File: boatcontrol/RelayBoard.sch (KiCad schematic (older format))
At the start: 15 parts, among them J2301 Conn_02x20_Odd_Even Header, J2302 TBL008V-1000-08BE, J2303 TBL008V-1000-08BE, K2301 EW60-1A3-CL12D04, K2302 EW60-1A3-CL12D04, K2303 EW60-1A3-CL12D04, K2304 EW60-1A3-CL12D04, K2305 EW60-1A3-CL12D04, K2306 EW60-1A3-CL12D04, K2307 EW60-1A3-CL12D04, K2308 EW60-1A3-CL12D04

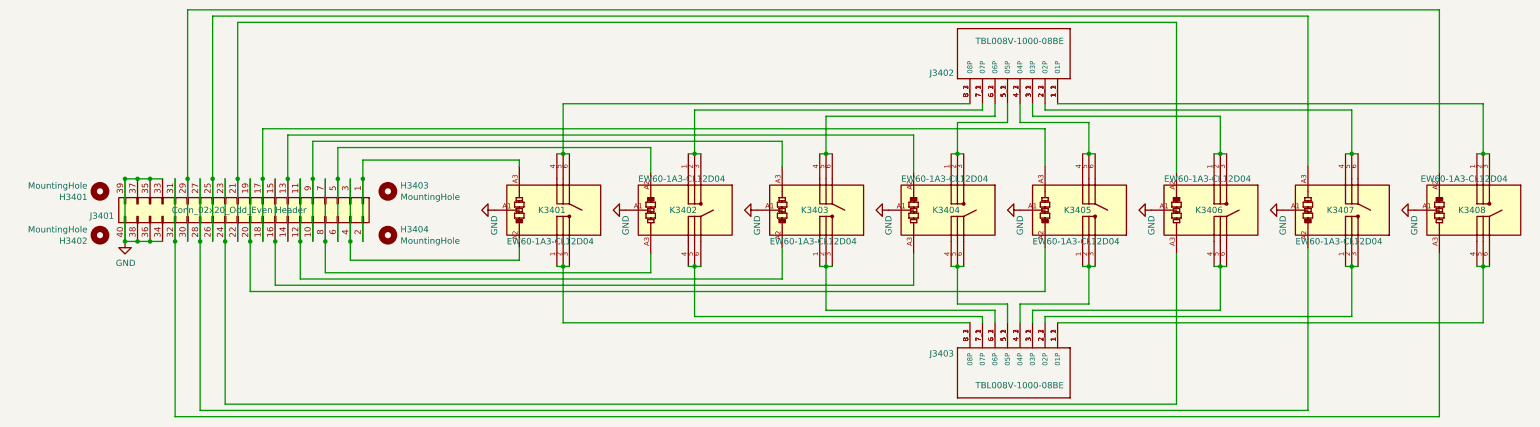
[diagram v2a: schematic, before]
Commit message: Fix extra signals
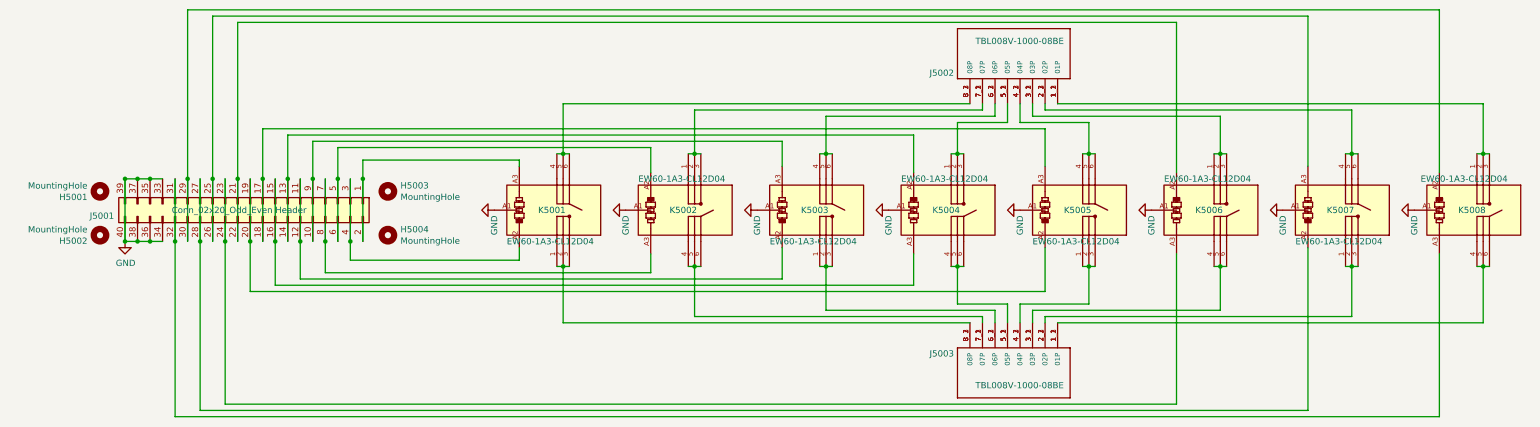
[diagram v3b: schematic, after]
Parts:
- renumbered H2301 to H5001, H2302 to H5002, H2303 to H5003, H2304 to H5004, J2301 to J5001, J2302 to J5002, J2303 to J5003, K2301 to K5001, K2302 to K5002, K2303 to K5003, K2304 to K5004, K2305 to K5005, K2306 to K5006, K2307 to K5007, K2308 to K5008

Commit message: CRC ErrorFree
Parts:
- renumbered H5003 to H5002, H5002 to H5003, J5002 to J5001, J5001 to J5002, K5002 to K5001, K5004 to K5002, K5006 to K5003, K5008 to K5004, K5001 to K5005, K5003 to K5006, K5005 to K5007, K5007 to K5008
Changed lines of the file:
@@
 AR Path="/E0EE2714/E107FCD3/E1098DA6" Ref="#PWR?"  Part="1"
 AR Path="/E171B338/E1098DA6" Ref="#PWR?"  Part="1"
-AR Path="/E171B33C/5F80BAC6/E1098DA6" Ref="#PWR05002"  Part="1"
-F 0 "#PWR05002" H 3200 3800 50  0001 C CNN
+AR Path="/E171B33C/5F80BAC6/E1098DA6" Ref="#PWR05001"  Part="1"
+F 0 "#PWR05001" H 3200 3800 50  0001 C CNN
 F 1 "GND" H 3400 4050 50  0000 R CNN
 F 2 "" H 3200 4050 50  0001 C CNN
@@
 AR Path="/E0EE2714/E107FCD3/E1098DAC" Ref="#PWR?"  Part="1"
 AR Path="/E171B338/E1098DAC" Ref="#PWR?"  Part="1"
-AR Path="/E171B33C/5F80BAC6/E1098DAC" Ref="#PWR05003"  Part="1"
-F 0 "#PWR05003" H 4250 3800 50  0001 C CNN
+AR Path="/E171B33C/5F80BAC6/E1098DAC" Ref="#PWR05002"  Part="1"
+F 0 "#PWR05002" H 4250 3800 50  0001 C CNN
 F 1 "GND" H 4450 4050 50  0000 R CNN
 F 2 "" H 4250 4050 50  0001 C CNN
@@
 AR Path="/E0EE2714/E107FCD3/E1098DB2" Ref="#PWR?"  Part="1"
 AR Path="/E171B338/E1098DB2" Ref="#PWR?"  Part="1"
-AR Path="/E171B33C/5F80BAC6/E1098DB2" Ref="#PWR05004"  Part="1"
-F 0 "#PWR05004" H 5300 3800 50  0001 C CNN
+AR Path="/E171B33C/5F80BAC6/E1098DB2" Ref="#PWR05003"  Part="1"
+F 0 "#PWR05003" H 5300 3800 50  0001 C CNN
 F 1 "GND" H 5500 4050 50  0000 R CNN
 F 2 "" H 5300 4050 50  0001 C CNN
@@
 AR Path="/E0EE2714/E107FCD3/E1098DB8" Ref="#PWR?"  Part="1"
 AR Path="/E171B338/E1098DB8" Ref="#PWR?"  Part="1"
-AR Path="/E171B33C/5F80BAC6/E1098DB8" Ref="#PWR05005"  Part="1"
-F 0 "#PWR05005" H 6350 3800 50  0001 C CNN
+AR Path="/E171B33C/5F80BAC6/E1098DB8" Ref="#PWR05004"  Part="1"
+F 0 "#PWR05004" H 6350 3800 50  0001 C CNN
 F 1 "GND" H 6550 4050 50  0000 R CNN
 F 2 "" H 6350 4050 50  0001 C CNN
@@
 AR Path="/E0EE2714/E107FCD3/E1098DC4" Ref="#PWR?"  Part="1"
 AR Path="/E171B338/E1098DC4" Ref="#PWR?"  Part="1"
-AR Path="/E171B33C/5F80BAC6/E1098DC4" Ref="#PWR05007"  Part="1"
-F 0 "#PWR05007" H 8450 3800 50  0001 C CNN
+AR Path="/E171B33C/5F80BAC6/E1098DC4" Ref="#PWR05006"  Part="1"
+F 0 "#PWR05006" H 8450 3800 50  0001 C CNN
 F 1 "GND" H 8650 4050 50  0000 R CNN
 F 2 "" H 8450 4050 50  0001 C CNN
@@
 AR Path="/E0EE2714/E107FCD3/E1098DCA" Ref="#PWR?"  Part="1"
 AR Path="/E171B338/E1098DCA" Ref="#PWR?"  Part="1"
-AR Path="/E171B33C/5F80BAC6/E1098DCA" Ref="#PWR05008"  Part="1"
-F 0 "#PWR05008" H 9500 3800 50  0001 C CNN
+AR Path="/E171B33C/5F80BAC6/E1098DCA" Ref="#PWR05007"  Part="1"
+F 0 "#PWR05007" H 9500 3800 50  0001 C CNN
 F 1 "GND" H 9700 4050 50  0000 R CNN
 F 2 "" H 9500 4050 50  0001 C CNN
@@
 AR Path="/E0EE2714/E107FCD3/E1098DD0" Ref="#PWR?"  Part="1"
 AR Path="/E171B338/E1098DD0" Ref="#PWR?"  Part="1"
-AR Path="/E171B33C/5F80BAC6/E1098DD0" Ref="#PWR05009"  Part="1"
-F 0 "#PWR05009" H 10550 3800 50  0001 C CNN
+AR Path="/E171B33C/5F80BAC6/E1098DD0" Ref="#PWR05008"  Part="1"
+F 0 "#PWR05008" H 10550 3800 50  0001 C CNN
 F 1 "GND" H 10750 4050 50  0000 R CNN
 F 2 "" H 10550 4050 50  0001 C CNN
@@
 AR Path="/E0EE2714/E107FCD3/E1098DE2" Ref="J?"  Part="1"
 AR Path="/E171B338/E1098DE2" Ref="J?"  Part="1"
-AR Path="/E171B33C/5F80BAC6/E1098DE2" Ref="J5002"  Part="1"
-F 0 "J5002" V 7146 2372 50  0000 R CNN
+AR Path="/E171B33C/5F80BAC6/E1098DE2" Ref="J5001"  Part="1"
+F 0 "J5001" V 7146 2372 50  0000 R CNN
 F 1 "TBL008V-1000-08BE" V 7400 3250 50  0000 R CNN
 F 2 "CUI_TBL008V-1000-08BE" H 7300 2800 50  0001 L BNN
@@
 AR Path="/E0EE2714/E107FCD3/E1098DE8" Ref="K?"  Part="1"
 AR Path="/E171B338/E1098DE8" Ref="K?"  Part="1"
-AR Path="/E171B33C/5F80BAC6/E1098DE8" Ref="K5002"  Part="1"
-F 0 "K5002" V 4800 3850 50  0000 L CNN
+AR Path="/E171B33C/5F80BAC6/E1098DE8" Ref="K5001"  Part="1"
+F 0 "K5001" V 4800 3850 50  0000 L CNN
 F 1 "EW60-1A3-CL12D04" V 4550 3600 50  0000 L CNN
 F 2 "BoatControl:TE_2071366-2" H 4750 4400 50  0001 L BNN
@@
 AR Path="/E0EE2714/E107FCD3/E1098DF4" Ref="K?"  Part="1"
 AR Path="/E171B338/E1098DF4" Ref="K?"  Part="1"
-AR Path="/E171B33C/5F80BAC6/E1098DF4" Ref="K5004"  Part="1"
-F 0 "K5004" V 6900 3850 50  0000 L CNN
+AR Path="/E171B33C/5F80BAC6/E1098DF4" Ref="K5002"  Part="1"
+F 0 "K5002" V 6900 3850 50  0000 L CNN
 F 1 "EW60-1A3-CL12D04" V 6650 3600 50  0000 L CNN
 F 2 "BoatControl:TE_2071366-2" H 6850 4400 50  0001 L BNN
@@
 AR Path="/E0EE2714/E107FCD3/E1098E00" Ref="K?"  Part="1"
 AR Path="/E171B338/E1098E00" Ref="K?"  Part="1"
-AR Path="/E171B33C/5F80BAC6/E1098E00" Ref="K5006"  Part="1"
-F 0 "K5006" V 9000 3850 50  0000 L CNN
+AR Path="/E171B33C/5F80BAC6/E1098E00" Ref="K5003"  Part="1"
+F 0 "K5003" V 9000 3850 50  0000 L CNN
 F 1 "EW60-1A3-CL12D04" V 8750 3600 50  0000 L CNN
 F 2 "BoatControl:TE_2071366-2" H 8950 4400 50  0001 L BNN
@@
 AR Path="/E0EE2714/E107FCD3/E1098E0C" Ref="K?"  Part="1"
 AR Path="/E171B338/E1098E0C" Ref="K?"  Part="1"
-AR Path="/E171B33C/5F80BAC6/E1098E0C" Ref="K5008"  Part="1"
-F 0 "K5008" V 11100 3850 50  0000 L CNN
+AR Path="/E171B33C/5F80BAC6/E1098E0C" Ref="K5004"  Part="1"
+F 0 "K5004" V 11100 3850 50  0000 L CNN
 F 1 "EW60-1A3-CL12D04" V 10850 3550 50  0000 L CNN
 F 2 "BoatControl:TE_2071366-2" H 11050 4400 50  0001 L BNN
@@
 AR Path="/E0EE2714/E107FCD3/5F4F4DC8" Ref="#PWR?"  Part="1"
 AR Path="/E171B338/5F4F4DC8" Ref="#PWR?"  Part="1"
-AR Path="/E171B33C/5F80BAC6/5F4F4DC8" Ref="#PWR05006"  Part="1"
-F 0 "#PWR05006" H 7400 3800 50  0001 C CNN
+AR Path="/E171B33C/5F80BAC6/5F4F4DC8" Ref="#PWR05005"  Part="1"
+F 0 "#PWR05005" H 7400 3800 50  0001 C CNN
 F 1 "GND" H 7600 4050 50  0000 R CNN
 F 2 "" H 7400 4050 50  0001 C CNN
@@
 AR Path="/E0EE2714/E107FCD3/E1098E86" Ref="H?"  Part="1"
 AR Path="/E171B338/E1098E86" Ref="H?"  Part="1"
-AR Path="/E171B33C/5F80BAC6/E1098E86" Ref="H5003"  Part="1"
-F 0 "H5003" H 2450 3946 50  0000 L CNN
+AR Path="/E171B33C/5F80BAC6/E1098E86" Ref="H5002"  Part="1"
+F 0 "H5002" H 2450 3946 50  0000 L CNN
 F 1 "MountingHole" H 2450 3855 50  0000 L CNN
 F 2 "MountingHole:MountingHole_3mm" H 2350 3900 50  0001 C CNN
@@
 AR Path="/E0EE2714/E107FCD3/E1098E7A" Ref="H?"  Part="1"
 AR Path="/E171B338/E1098E7A" Ref="H?"  Part="1"
-AR Path="/E171B33C/5F80BAC6/E1098E7A" Ref="H5002"  Part="1"
-F 0 "H5002" H 150 4296 50  0000 L CNN
+AR Path="/E171B33C/5F80BAC6/E1098E7A" Ref="H5003"  Part="1"
+F 0 "H5003" H 150 4296 50  0000 L CNN
 F 1 "MountingHole" H 150 4205 50  0000 L CNN
 F 2 "MountingHole:MountingHole_3mm" H 50  4250 50  0001 C CNN
@@
 AR Path="/E0EE2714/E107FCD3/E1098E06" Ref="K?"  Part="1"
 AR Path="/E171B338/E1098E06" Ref="K?"  Part="1"
-AR Path="/E171B33C/5F80BAC6/E1098E06" Ref="K5007"  Part="1"
-F 0 "K5007" V 10050 3950 50  0000 L CNN
+AR Path="/E171B33C/5F80BAC6/E1098E06" Ref="K5008"  Part="1"
+F 0 "K5008" V 10050 3950 50  0000 L CNN
 F 1 "EW60-1A3-CL12D04" V 9800 3700 50  0000 L CNN
 F 2 "BoatControl:TE_2071366-2" H 10000 4500 50  0001 L BNN
@@
 AR Path="/E0EE2714/E107FCD3/E1098DFA" Ref="K?"  Part="1"
 AR Path="/E171B338/E1098DFA" Ref="K?"  Part="1"
-AR Path="/E171B33C/5F80BAC6/E1098DFA" Ref="K5005"  Part="1"
-F 0 "K5005" V 7950 3950 50  0000 L CNN
+AR Path="/E171B33C/5F80BAC6/E1098DFA" Ref="K5007"  Part="1"
+F 0 "K5007" V 7950 3950 50  0000 L CNN
 F 1 "EW60-1A3-CL12D04" V 7700 3700 50  0000 L CNN
 F 2 "BoatControl:TE_2071366-2" H 7900 4500 50  0001 L BNN
@@
 AR Path="/E0EE2714/E107FCD3/E1098DEE" Ref="K?"  Part="1"
 AR Path="/E171B338/E1098DEE" Ref="K?"  Part="1"
-AR Path="/E171B33C/5F80BAC6/E1098DEE" Ref="K5003"  Part="1"
-F 0 "K5003" V 5850 3950 50  0000 L CNN
+AR Path="/E171B33C/5F80BAC6/E1098DEE" Ref="K5006"  Part="1"
+F 0 "K5006" V 5850 3950 50  0000 L CNN
 F 1 "EW60-1A3-CL12D04" V 5600 3700 50  0000 L CNN
 F 2 "BoatControl:TE_2071366-2" H 5800 4500 50  0001 L BNN
@@
 AR Path="/E0EE2714/E107FCD3/E1098E92" Ref="K?"  Part="1"
 AR Path="/E171B338/E1098E92" Ref="K?"  Part="1"
-AR Path="/E171B33C/5F80BAC6/E1098E92" Ref="K5001"  Part="1"
-F 0 "K5001" V 3750 3950 50  0000 L CNN
+AR Path="/E171B33C/5F80BAC6/E1098E92" Ref="K5005"  Part="1"
+F 0 "K5005" V 3750 3950 50  0000 L CNN
 F 1 "EW60-1A3-CL12D04" V 3500 3700 50  0000 L CNN
 F 2 "BoatControl:TE_2071366-2" H 3700 4500 50  0001 L BNN
@@
 AR Path="/E0EE2714/E107FCD3/E1098E6E" Ref="J?"  Part="1"
 AR Path="/E171B338/E1098E6E" Ref="J?"  Part="1"
-AR Path="/E171B33C/5F80BAC6/E1098E6E" Ref="J5001"  Part="1"
-F 0 "J5001" V 1346 2913 50  0000 R CNN
+AR Path="/E171B33C/5F80BAC6/E1098E6E" Ref="J5002"  Part="1"
+F 0 "J5002" V 1346 2913 50  0000 R CNN
 F 1 "Conn_02x20_Odd_Even Header" V 1300 4450 50  0000 R CNN
 F 2 "Connector_PinSocket_2.54mm:PinSocket_2x20_P2.54mm_Vertical" H 1250 4000 50  0001 C CNN
@@
 Connection ~ 250  4300
 $Comp
-L power:GND #PWR05001
+L power:GND #PWR05009
 U 1 1 60E5FB29
 P 250 4300
-F 0 "#PWR05001" H 250 4050 50  0001 C CNN
+F 0 "#PWR05009" H 250 4050 50  0001 C CNN
 F 1 "GND" H 255 4127 50  0000 C CNN
 F 2 "" H 250 4300 50  0001 C CNN

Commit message: Fix graphics
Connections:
- net K4_OUT: now reaches J5003.1_1 (01P), J5003.1_2 (01P), J5003.1_3 (01P), K5004.4, K5004.5, K5004.6
- net K8_OUT: now reaches J5003.2_1 (02P), J5003.2_2 (02P), J5003.2_3 (02P), K5008.1, K5008.2, K5008.3
- net K3_OUT: now reaches J5003.3_1 (03P), J5003.3_2 (03P), J5003.3_3 (03P), K5003.4, K5003.5, K5003.6
- net K7_OUT: now reaches J5003.4_1 (04P), J5003.4_2 (04P), J5003.4_3 (04P), K5007.1, K5007.2, K5007.3
- net K2_OUT: now reaches J5003.5_1 (05P), J5003.5_2 (05P), J5003.5_3 (05P), K5002.4, K5002.5, K5002.6
- net K6_OUT: now reaches J5003.6_1 (06P), J5003.6_2 (06P), J5003.6_3 (06P), K5006.1, K5006.2, K5006.3
- net K1_OUT: now reaches J5003.7_1 (07P), J5003.7_2 (07P), J5003.7_3 (07P), K5001.4, K5001.5, K5001.6
- net K5_OUT: now reaches J5003.8_1 (08P), J5003.8_2 (08P), J5003.8_3 (08P), K5005.1, K5005.2, K5005.3
- net K4_IN: now reaches J5001.1_1 (01P), J5001.1_2 (01P), J5001.1_3 (01P), K5004.1, K5004.2, K5004.3
- net K8_IN: now reaches J5001.2_1 (02P), J5001.2_2 (02P), J5001.2_3 (02P), K5008.4, K5008.5, K5008.6
- net K3_IN: now reaches J5001.3_1 (03P), J5001.3_2 (03P), J5001.3_3 (03P), K5003.1, K5003.2, K5003.3
- net K7_IN: now reaches J5001.4_1 (04P), J5001.4_2 (04P), J5001.4_3 (04P), K5007.4, K5007.5, K5007.6
- net K2_IN: now reaches J5001.5_1 (05P), J5001.5_2 (05P), J5001.5_3 (05P), K5002.1, K5002.2, K5002.3
- net K6_IN: now reaches J5001.6_1 (06P), J5001.6_2 (06P), J5001.6_3 (06P), K5006.4, K5006.5, K5006.6
- net K1_IN: now reaches J5001.7_1 (07P), J5001.7_2 (07P), J5001.7_3 (07P), K5001.1, K5001.2, K5001.3
- net K5_IN: now reaches J5001.8_1 (08P), J5001.8_2 (08P), J5001.8_3 (08P), K5005.4, K5005.5, K5005.6
- net K2_COIL_OFF: now reaches J5002.5 (Pin_5), J5002.6 (Pin_6), K5001.A2
- net K2_COIL_OFF: now also J5002.13 (Pin_13), J5002.14 (Pin_14), K5002.A2
- net K1_COIL_ON: now reaches J5002.7 (Pin_7), J5002.8 (Pin_8), K5001.A3
- net K6_COIL_ON: now reaches J5002.11 (Pin_11), J5002.12 (Pin_12), K5006.A2
- net K6_COIL_OFF: now reaches J5002.10 (Pin_10), J5002.9 (Pin_9), K5006.A3
- net K2_COIL_ON: now reaches J5002.15 (Pin_15), J5002.16 (Pin_16), K5002.A3
- net K7_COIL_ON: now reaches J5002.19 (Pin_19), J5002.20 (Pin_20), K5007.A2
- net K7_COIL_OFF: now reaches J5002.17 (Pin_17), J5002.18 (Pin_18), K5007.A3
- net K3_COIL_OFF: now reaches J5002.21 (Pin_21), J5002.22 (Pin_22), K5003.A2
- net K3_COIL_ON: now reaches J5002.23 (Pin_23), J5002.24 (Pin_24), K5003.A3
- net K8_COIL_ON: now reaches J5002.27 (Pin_27), J5002.28 (Pin_28), K5008.A2
- net K8_COIL_ON: now also J5002.31 (Pin_31), J5002.32 (Pin_32), K5004.A3
- net K8_COIL_OFF: now reaches J5002.25 (Pin_25), J5002.26 (Pin_26), K5008.A3
- net K4_COIL_OFF: now reaches J5002.29 (Pin_29), J5002.30 (Pin_30), K5004.A2
- net K5_COIL_OFF: now reaches J5002.1 (Pin_1), J5002.2 (Pin_2), K5005.A3
- net K5_COIL_ON: now reaches J5002.3 (Pin_3), J5002.4 (Pin_4), K5005.A2
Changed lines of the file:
@@
 	1    0    0    -1
 $EndComp
+Text Label 4800 3350 0    50   ~ 0
+K1_IN
+Text Label 3750 3350 0    50   ~ 0
+K5_IN
+Text Label 5850 3550 0    50   ~ 0
+K6_IN
+Text Label 6900 3550 0    50   ~ 0
+K2_IN
+Text Label 7950 3550 0    50   ~ 0
+K7_IN
+Text Label 9000 3550 0    50   ~ 0
+K3_IN
+Text Label 10050 3550 0    50   ~ 0
+K8_IN
+Text Label 11100 3550 0    50   ~ 0
+K4_IN
+Text Label 3750 4850 0    50   ~ 0
+K5_OUT
+Text Label 4800 4850 0    50   ~ 0
+K1_OUT
+Text Label 5850 4800 0    50   ~ 0
+K6_OUT
+Text Label 6900 4650 0    50   ~ 0
+K2_OUT
+Text Label 7950 4650 0    50   ~ 0
+K7_OUT
+Text Label 9000 4650 0    50   ~ 0
+K3_OUT
+Text Label 10050 4650 0    50   ~ 0
+K8_OUT
+Text Label 11100 4650 0    50   ~ 0
+K4_OUT
+Text Label 4450 4500 2    50   ~ 0
+K1_COIL_ON
+Text Label 5500 4500 2    50   ~ 0
+K6_COIL_ON
+Text Label 6550 4500 2    50   ~ 0
+K2_COIL_ON
+Text Label 4450 3700 2    50   ~ 0
+K2_COIL_OFF
+Text Label 5500 3700 2    50   ~ 0
+K6_COIL_OFF
+Text Label 6550 3700 2    50   ~ 0
+K2_COIL_OFF
+Text Label 7600 3700 2    50   ~ 0
+K7_COIL_OFF
+Text Label 7600 4500 2    50   ~ 0
+K7_COIL_ON
+Text Label 8650 4500 2    50   ~ 0
+K3_COIL_ON
+Text Label 8650 3700 2    50   ~ 0
+K3_COIL_OFF
+Text Label 9700 4500 2    50   ~ 0
+K8_COIL_ON
+Text Label 9700 3700 2    50   ~ 0
+K8_COIL_OFF
+Text Label 10750 3700 2    50   ~ 0
+K4_COIL_OFF
+Text Label 10750 4500 2    50   ~ 0
+K8_COIL_ON
+Text Label 3400 3650 2    50   ~ 0
+K5_COIL_OFF
+Text Label 3400 4450 2    50   ~ 0
+K5_COIL_ON
 $EndSCHEMATC

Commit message: Make 12V PSU Optional
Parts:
- K5005: Manufacturer (none) -> TE Connectivit
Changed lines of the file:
@@
 F 2 "BoatControl:TE_2071366-2" H 3700 4500 50  0001 L BNN
 F 3 "https://www.te.com/commerce/DocumentDelivery/DDEController?Action=srchrtrv&DocNm=EW60_Datasheet_07042016&DocType=DS&DocLang=English" H 4700 4600 50  0001 L BNN
+F 4 "TE Connectivit" V 3700 4100 50  0001 C CNN "Manufacturer"
 	1    3700 4100
 	0    1    -1   0
